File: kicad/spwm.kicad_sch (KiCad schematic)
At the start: 24 parts, among them J10 To IGBTs, J9 SPWM Driver Board, Q3 S8050, Q4 TIP125, U7 EL817, U8 LM7805_TO220

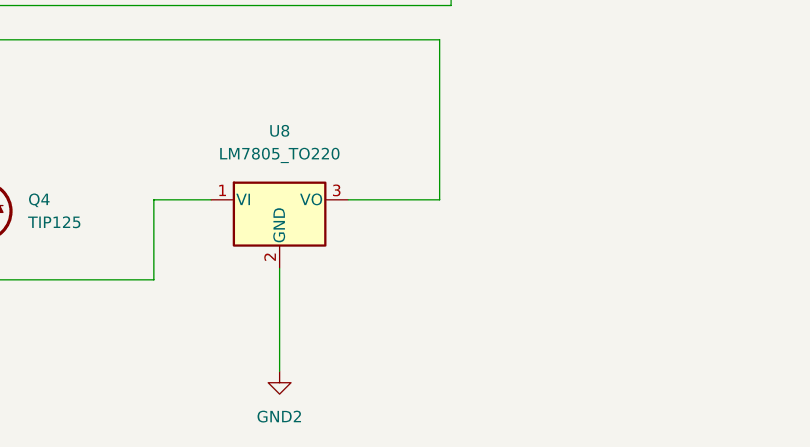
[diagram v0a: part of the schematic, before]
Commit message: Cambio Arduino por el ATMega328
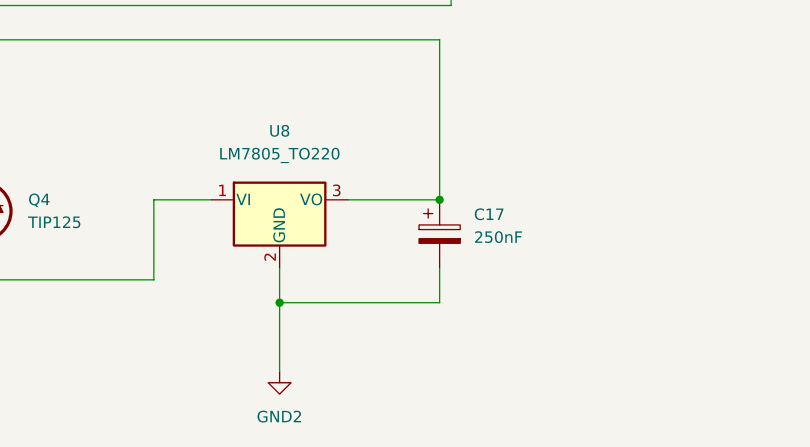
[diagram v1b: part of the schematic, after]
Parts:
- added C17: 250nF, Capacitor_THT:CP_Radial_D5.0mm_P2.50mm, symbol Device:C_Polarized
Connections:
- net 5v: now also C17.1
- net GND2: now also C17.2
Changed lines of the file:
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@@
   (junction (at 130.81 45.72) (diameter 0) (color 0 0 0 0)
   )
+  (junction (at 158.75 123.19) (diameter 0) (color 0 0 0 0)
+  )
   (junction (at 85.09 45.72) (diameter 0) (color 0 0 0 0)
+  )
+  (junction (at 140.97 134.62) (diameter 0) (color 0 0 0 0)
   )
   (junction (at 77.47 72.39) (diameter 0) (color 0 0 0 0)
@@
     (stroke (width 0) (type default) (color 0 0 0 0))
   )
+  (wire (pts (xy 140.97 134.62) (xy 140.97 142.24))
+    (stroke (width 0) (type default) (color 0 0 0 0))
+  )
   (wire (pts (xy 109.22 132.08) (xy 127 132.08))
     (stroke (width 0) (type default) (color 0 0 0 0))
@@
     (stroke (width 0) (type default) (color 0 0 0 0))
   )
-  (wire (pts (xy 140.97 142.24) (xy 140.97 130.81))
+  (wire (pts (xy 140.97 130.81) (xy 140.97 134.62))
     (stroke (width 0) (type default) (color 0 0 0 0))
   )
@@
   )
   (wire (pts (xy 39.37 31.75) (xy 39.37 107.95))
+    (stroke (width 0) (type default) (color 0 0 0 0))
+  )
+  (wire (pts (xy 158.75 134.62) (xy 140.97 134.62))
+    (stroke (width 0) (type default) (color 0 0 0 0))
+  )
+  (wire (pts (xy 158.75 130.81) (xy 158.75 134.62))
     (stroke (width 0) (type default) (color 0 0 0 0))
   )
@@
       (effects (font (size 1.27 1.27)) hide)
     )
+    (pin "1")
+    (pin "2")
+  )
+  (symbol (lib_id "Device:C_Polarized") (at 158.75 127 0) (unit 1)
+    (in_bom yes) (on_board yes) (fields_autoplaced)
+    (property "Reference" "C17" (id 0) (at 162.56 124.8409 0)
+      (effects (font (size 1.27 1.27)) (justify left))
+    )
+    (property "Value" "250nF" (id 1) (at 162.56 127.3809 0)
+      (effects (font (size 1.27 1.27)) (justify left))
+    )
+    (property "Footprint" "Capacitor_THT:CP_Radial_D5.0mm_P2.50mm" (id 2) (at 159.7152 130.81 0)
+      (effects (font (size 1.27 1.27)) hide)
+    )
+    (property "Datasheet" "~" (id 3) (at 158.75 127 0)
+      (effects (font (size 1.27 1.27)) hide)
+    )
